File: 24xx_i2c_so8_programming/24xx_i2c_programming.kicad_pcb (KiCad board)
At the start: 2 copper layers, 14 x 11.4 mm, 11 parts, among them J1 EXPANSION_BOTTOM, J2 A0, J3 A1, J4 A2, J5 WP, U1 24LC00

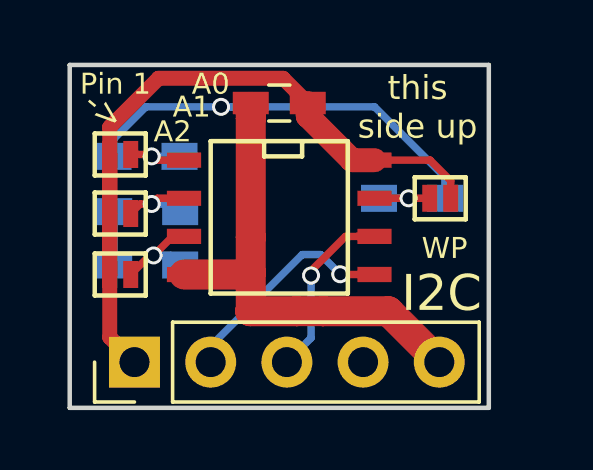
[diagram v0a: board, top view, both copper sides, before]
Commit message: Giving the 24xx SO8 board a new name, changing the passive footprints, adding +- on the silkscreen
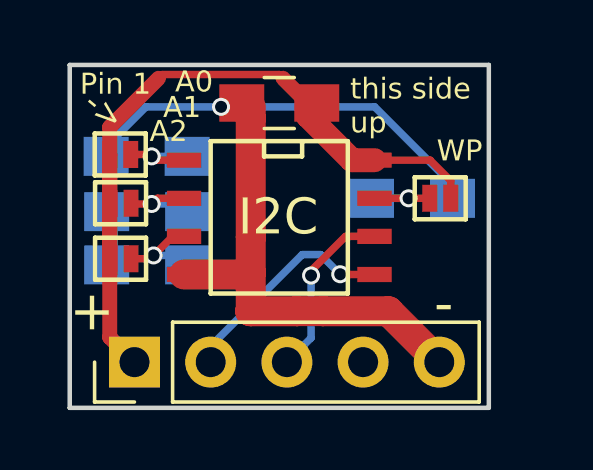
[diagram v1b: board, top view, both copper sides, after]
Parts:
- C1: footprint Capacitors_SMD:C_0603_HandSoldering -> Capacitors_SMD:C_0805_HandSoldering
- R1, R2, R3, R4: footprint Resistors_SMD:R_0603_HandSoldering -> Resistors_SMD:R_0805_HandSoldering
- moved J4 0.53 mm to (168.3, 117.0)
- moved J3 0.34 mm to (168.3, 115.1)
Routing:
- net GND: track 34.5 -> 35.2 mm
- net VCC: track 26.8 -> 27.5 mm
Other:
- board text added: "+"
- board text added: "-"
- board text added: "24xx SO8 EEPROM mod board"
- board text added: "v1.1"
- board text removed: "24xx EEPROM mod board"
- board text removed: "v1.0"
